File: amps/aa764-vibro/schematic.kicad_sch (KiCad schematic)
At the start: 49 parts, among them J1 vibrato pedal, T1 125P1B, T2 125A35A

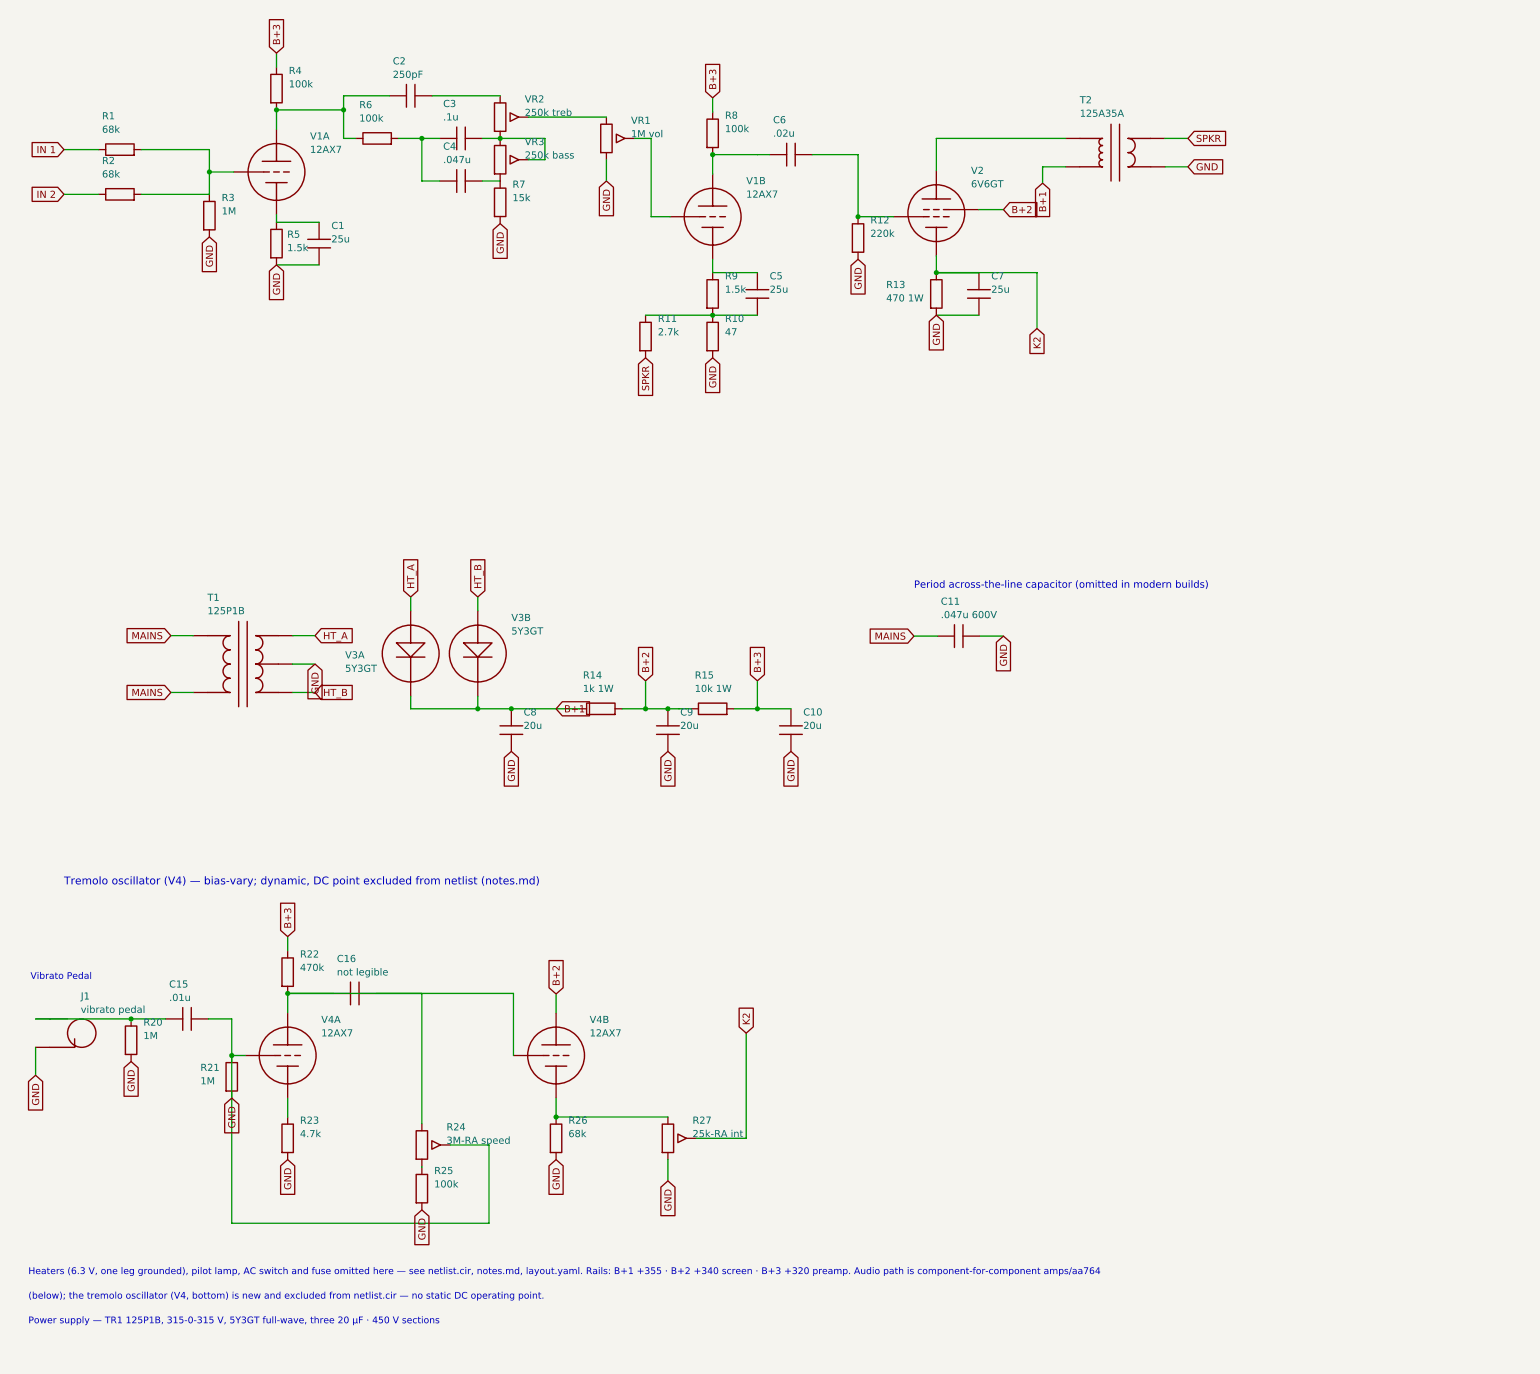
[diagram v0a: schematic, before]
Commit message: Fix: deterministic schematic ids and wires split at every join
- _u() is uuid5 over (amp id, emission order), so a regeneration of an
  unchanged script is byte-identical and a drift gate becomes possible
- write() splits wire segments at symbol pins, wire ends and junction dots,
  so the file connects exactly what the drawing shows under KiCad's
  endpoint-only semantics (270 pins were on a wire's interior; net
  partitions unchanged on all 38 sheets)
- all sheets regenerated; aa864-bassman title block was stale (draft) and
  now matches meta.yaml (verified)

Co-Authored-By: Claude Fable 5.1 <noreply@anthropic.com>
Claude-Session: https://claude.ai/code/session_01KBMfdh37HmCL2iWcBiL5J1
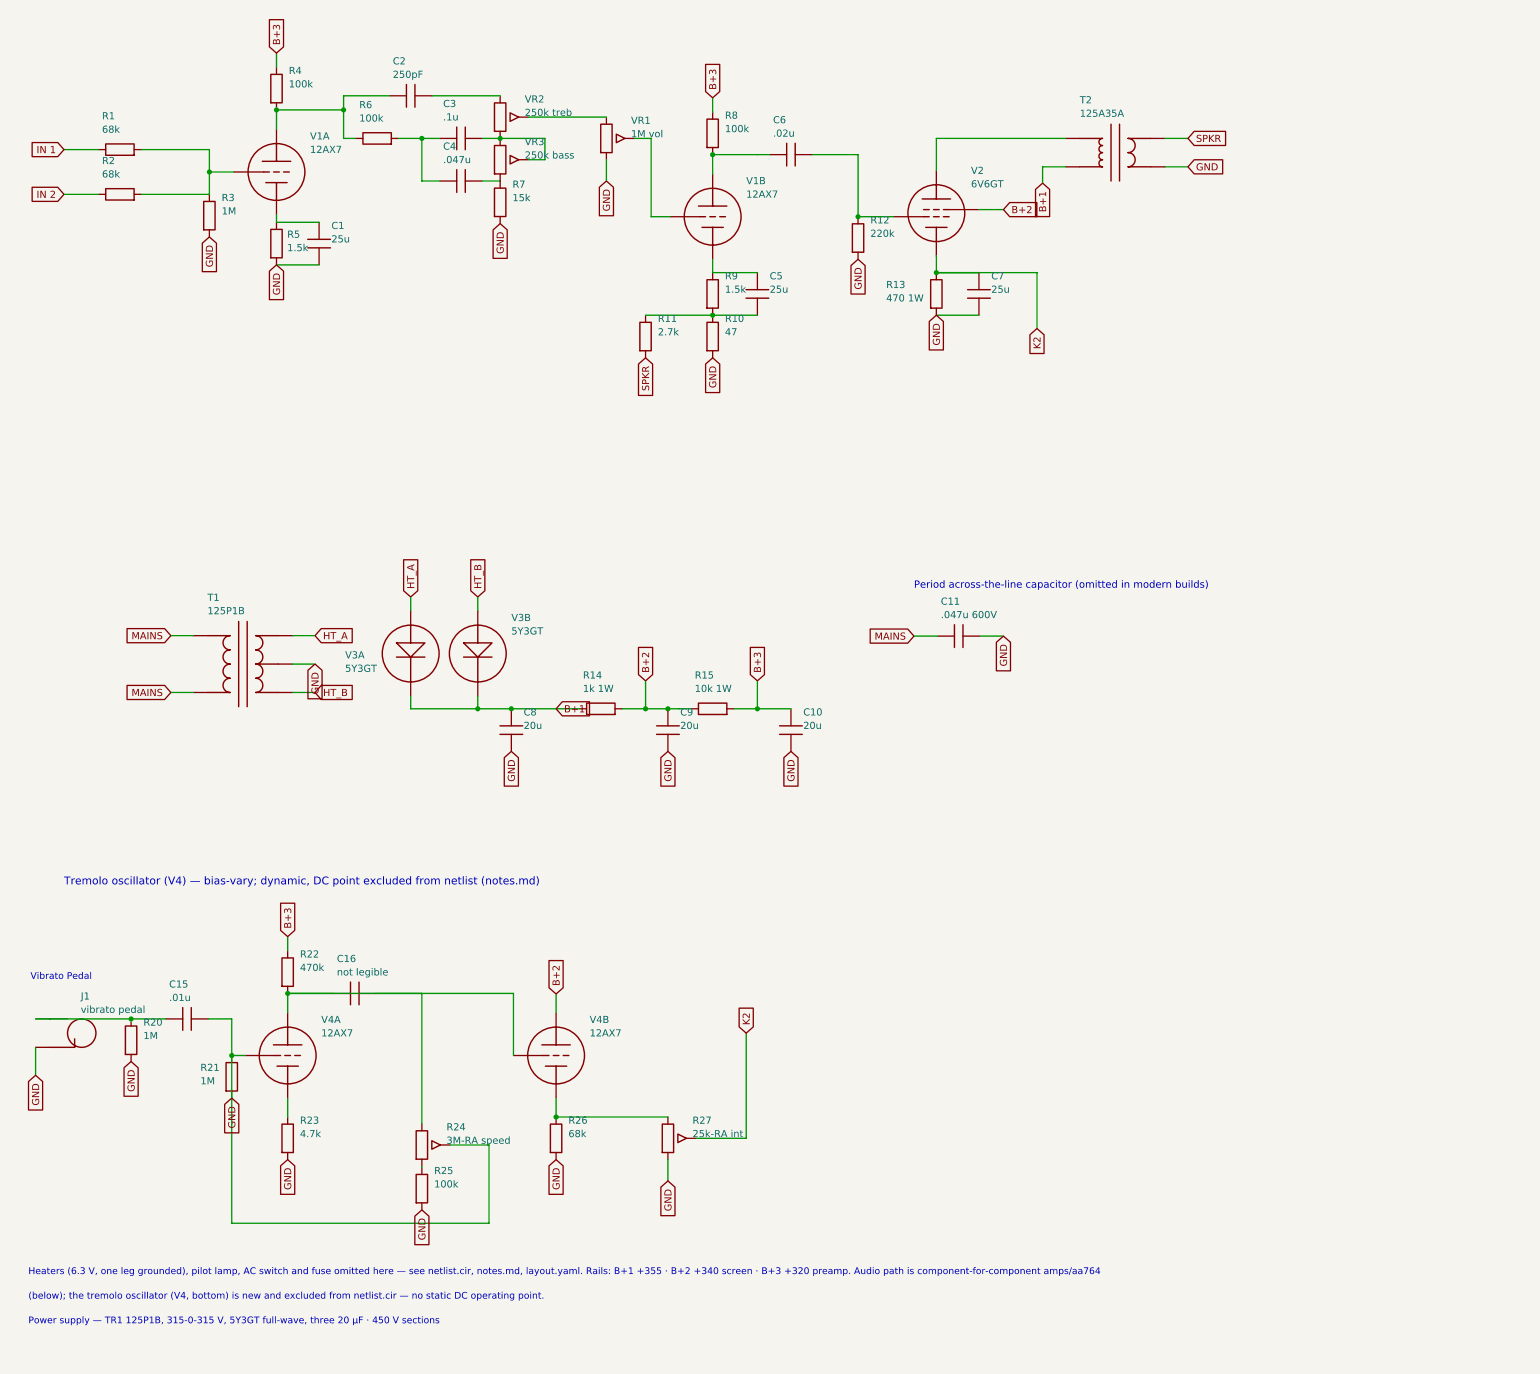
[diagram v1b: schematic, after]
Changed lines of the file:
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@@
   (wire (pts (xy 32.879 42.278) (xy 45.069 42.278))
     (stroke (width 0) (type default)))
-  (wire (pts (xy 45.069 34.278) (xy 45.069 42.278))
+  (wire (pts (xy 45.069 34.278) (xy 45.069 38.278))
+    (stroke (width 0) (type default)))
+  (wire (pts (xy 45.069 38.278) (xy 45.069 42.278))
     (stroke (width 0) (type default)))
   (junction (at 45.069 38.278) (diameter 0) (color 0 0 0 0))
@@
   (wire (pts (xy 57.069 27.178) (xy 69.069 27.178))
     (stroke (width 0) (type default)))
-  (wire (pts (xy 69.069 24.658) (xy 69.069 32.278))
+  (wire (pts (xy 69.069 24.658) (xy 69.069 27.178))
+    (stroke (width 0) (type default)))
+  (wire (pts (xy 69.069 27.178) (xy 69.069 32.278))
     (stroke (width 0) (type default)))
   (junction (at 69.069 27.178) (diameter 0) (color 0 0 0 0))
@@
     (effects (font (size 1.27 1.27)) (justify right)))
   (junction (at 175.069 56.278) (diameter 0) (color 0 0 0 0))
-  (wire (pts (xy 175.069 56.278) (xy 193.069 56.278))
+  (wire (pts (xy 175.069 56.278) (xy 182.689 56.278))
+    (stroke (width 0) (type default)))
+  (wire (pts (xy 182.689 56.278) (xy 193.069 56.278))
     (stroke (width 0) (type default)))
   (wire (pts (xy 193.069 56.278) (xy 193.069 66.278))
@@
   (wire (pts (xy 95.069 226.278) (xy 49.069 226.278))
     (stroke (width 0) (type default)))
-  (wire (pts (xy 49.069 226.278) (xy 49.069 196.278))
+  (wire (pts (xy 49.069 226.278) (xy 49.069 203.898))
+    (stroke (width 0) (type default)))
+  (wire (pts (xy 49.069 203.898) (xy 49.069 196.278))
     (stroke (width 0) (type default)))
   (symbol (lib_id "cx:TRIODE") (at 107.069 196.278 0) (unit 1)
@@
     (property "Reference" "V4B" (at 113.069 189.878 0) (effects (font (size 1.27 1.27)) (justify left)))
     (property "Value" "12AX7" (at 113.069 192.278 0) (effects (font (size 1.27 1.27)) (justify left))))
-  (wire (pts (xy 59.069 185.178) (xy 99.449 185.178))
+  (wire (pts (xy 59.069 185.178) (xy 67.259 185.178))
+    (stroke (width 0) (type default)))
+  (wire (pts (xy 67.259 185.178) (xy 74.879 185.178))
+    (stroke (width 0) (type default)))
+  (wire (pts (xy 74.879 185.178) (xy 83.069 185.178))
+    (stroke (width 0) (type default)))
+  (wire (pts (xy 83.069 185.178) (xy 99.449 185.178))
     (stroke (width 0) (type default)))
   (wire (pts (xy 99.449 185.178) (xy 99.449 196.278))
@@
   (wire (pts (xy 93.069 132.018) (xy 93.069 134.278))
     (stroke (width 0) (type default)))
-  (wire (pts (xy 81.069 134.278) (xy 107.069 134.278))
+  (wire (pts (xy 81.069 134.278) (xy 93.069 134.278))
+    (stroke (width 0) (type default)))
+  (wire (pts (xy 93.069 134.278) (xy 99.069 134.278))
+    (stroke (width 0) (type default)))
+  (wire (pts (xy 99.069 134.278) (xy 107.069 134.278))
     (stroke (width 0) (type default)))
   (junction (at 93.069 134.278) (diameter 0) (color 0 0 0 0))
@@
     (property "Reference" "R14" (at 111.869 128.278 270) (effects (font (size 1.27 1.27)) (justify left)))
     (property "Value" "1k 1W" (at 111.869 130.678 270) (effects (font (size 1.27 1.27)) (justify left))))
-  (wire (pts (xy 118.879 134.278) (xy 129.069 134.278))
+  (wire (pts (xy 118.879 134.278) (xy 123.069 134.278))
+    (stroke (width 0) (type default)))
+  (wire (pts (xy 123.069 134.278) (xy 127.069 134.278))
+    (stroke (width 0) (type default)))
+  (wire (pts (xy 127.069 134.278) (xy 129.069 134.278))
     (stroke (width 0) (type default)))
   (junction (at 123.069 134.278) (diameter 0) (color 0 0 0 0))
@@
     (property "Reference" "R15" (at 131.869 128.278 270) (effects (font (size 1.27 1.27)) (justify left)))
     (property "Value" "10k 1W" (at 131.869 130.678 270) (effects (font (size 1.27 1.27)) (justify left))))
-  (wire (pts (xy 138.879 134.278) (xy 149.069 134.278))
+  (wire (pts (xy 138.879 134.278) (xy 143.069 134.278))
+    (stroke (width 0) (type default)))
+  (wire (pts (xy 143.069 134.278) (xy 149.069 134.278))
     (stroke (width 0) (type default)))
   (junction (at 143.069 134.278) (diameter 0) (color 0 0 0 0))
